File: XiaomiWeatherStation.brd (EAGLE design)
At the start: 60 x 100 mm, 12 parts, among them K1 RELAY-SPDT, Q1 BD437

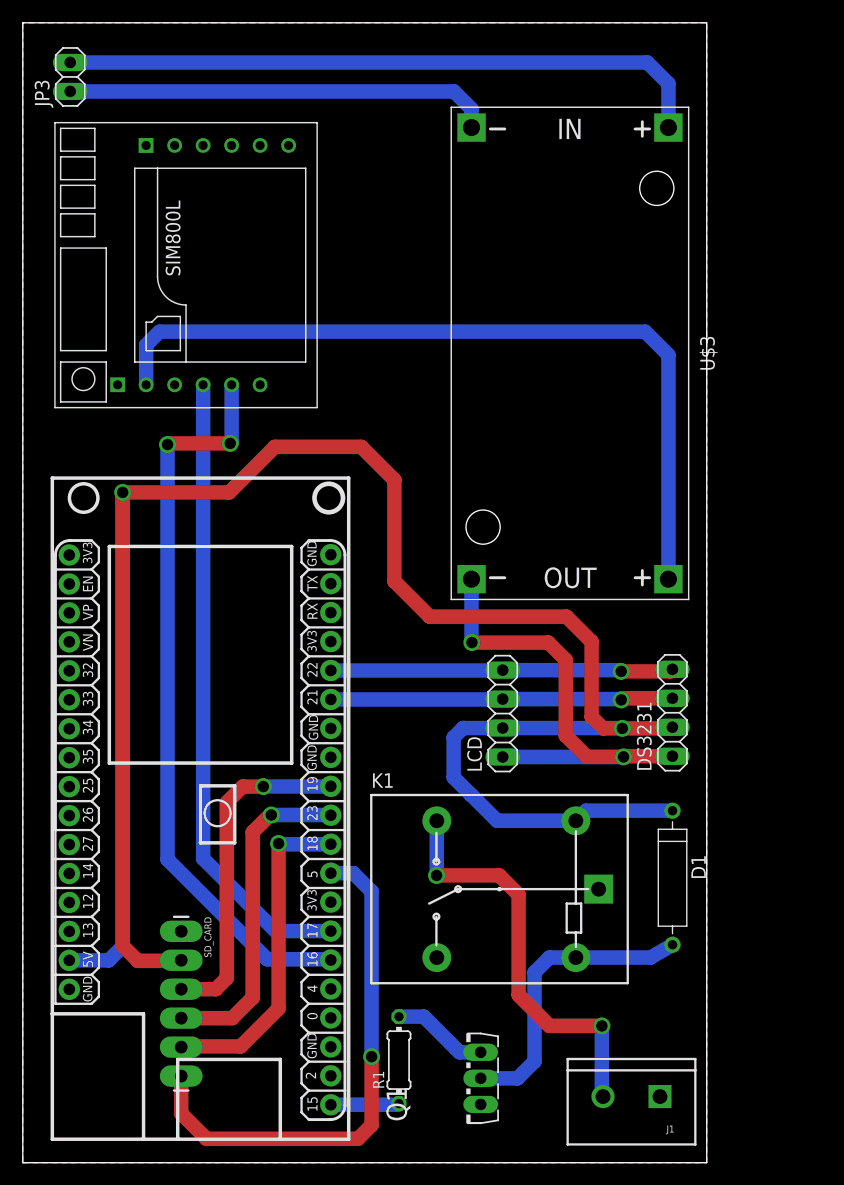
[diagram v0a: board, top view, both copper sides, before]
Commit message: Adds ground plane
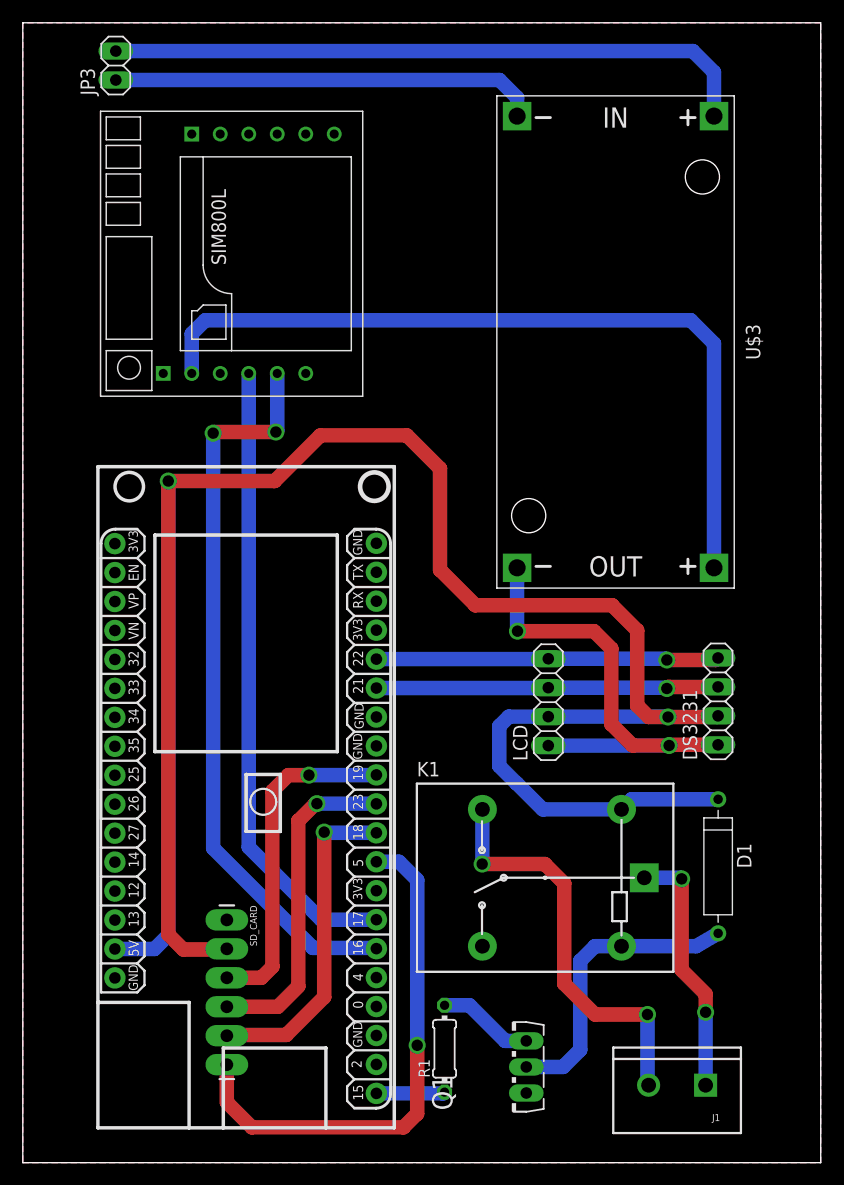
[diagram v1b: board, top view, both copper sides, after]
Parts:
- moved D1 4.12 mm to (61.0, 26.0)
- moved DS3231 4.12 mm to (61.0, 40.5)
- moved IC1 4.12 mm to (19.6, 36.6)
- moved J1 4.12 mm to (59.9, 6.80)
- moved JP3 4.12 mm to (8.16, 96.2)
- moved K1 4.12 mm to (46.0, 25.0)
- moved LCD 4.12 mm to (46.1, 40.4)
- moved Q1 4.12 mm to (42.9, 8.40)
- moved R1 4.12 mm to (37.0, 10.0)
- moved U$1 4.12 mm to (18.3, 79.7)
- moved U$3 4.12 mm to (52.0, 72.0)
- moved SD_CARD 4.12 mm to (17.9, 21.3)
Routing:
- net REL_COM: track 0.00 -> 22.3 mm, vias 0 -> 2
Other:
- board size 60 x 100 mm -> 70 x 100 mm
